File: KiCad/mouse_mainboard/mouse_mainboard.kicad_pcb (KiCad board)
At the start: 2 copper layers, 40.1 x 59.9 mm, 86 parts, among them J1 USB_OTG, J2 Conn_01x11_Male, Q1 BC807, Q10 BC807, Q11 BC817, Q12 BC807, Q13 BC817, Q14 BC817, Q2 BC807, Q3 BC817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

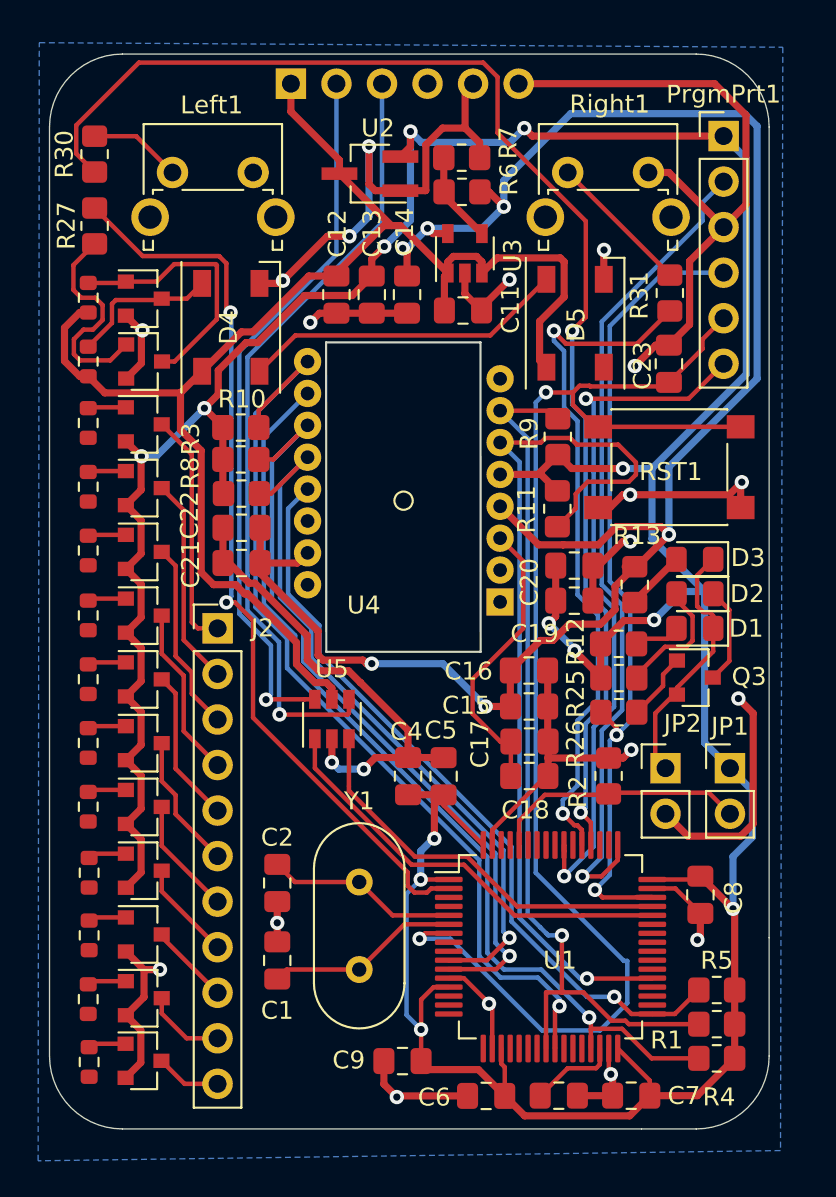
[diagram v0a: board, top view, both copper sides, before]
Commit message: Added test points
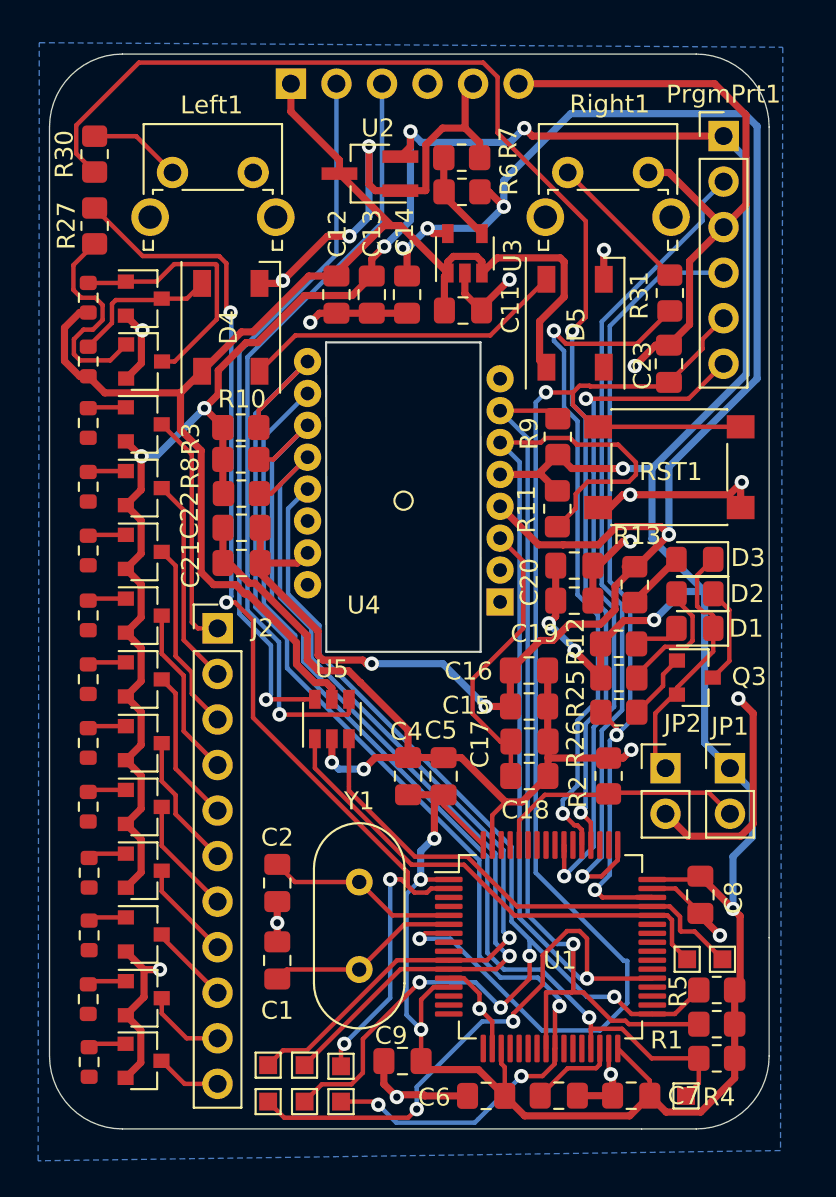
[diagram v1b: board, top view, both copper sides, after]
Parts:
- added TP1: TestPoint, TestPoint:TestPoint_Pad_1.0x1.0mm, F.Cu at (138.2, 128.5)
- added TP2: TestPoint, TestPoint:TestPoint_Pad_1.0x1.0mm, F.Cu at (136.1, 128.5)
- added TP3: TestPoint, TestPoint:TestPoint_Pad_1.0x1.0mm, F.Cu at (140.2, 130.6)
- added TP4: TestPoint, TestPoint:TestPoint_Pad_1.0x1.0mm, F.Cu at (136.1, 130.6)
- added TP5: TestPoint, TestPoint:TestPoint_Pad_1.0x1.0mm, F.Cu at (140.2, 128.6)
- added TP6: TestPoint, TestPoint:TestPoint_Pad_1.0x1.0mm, F.Cu at (159.5, 122.6)
- added TP7: TestPoint, TestPoint:TestPoint_Pad_1.0x1.0mm, F.Cu at (161.5, 122.6)
- added TP8: TestPoint, TestPoint:TestPoint_Pad_1.0x1.0mm, F.Cu at (159.4, 130.2)
- added TP9: TestPoint, TestPoint:TestPoint_Pad_1.0x1.0mm, F.Cu at (138.2, 130.6)
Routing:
- net pwm_gpo: track 50.8 -> 77.6 mm, vias 1 -> 3
- net ncs: track 42.9 -> 62.7 mm, vias 1 -> 4
- net pwm_int: track 52.7 -> 67.3 mm, vias 1 -> 3
- net led_d: track 50.6 -> 63.3 mm, vias 2 -> 4
- net miso: track 40.4 -> 52.9 mm
- net mosi: track 43.2 -> 53.4 mm
- net usb_d+: track 22.5 -> 28.1 mm
- net GND: track 182.1 -> 187.4 mm
- net usb_d-: track 23.9 -> 27.6 mm
- net sclk: track 53.0 -> 55.4 mm
- net mcu_cap: track 224.1 -> 225.9 mm

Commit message: Added pot strip port
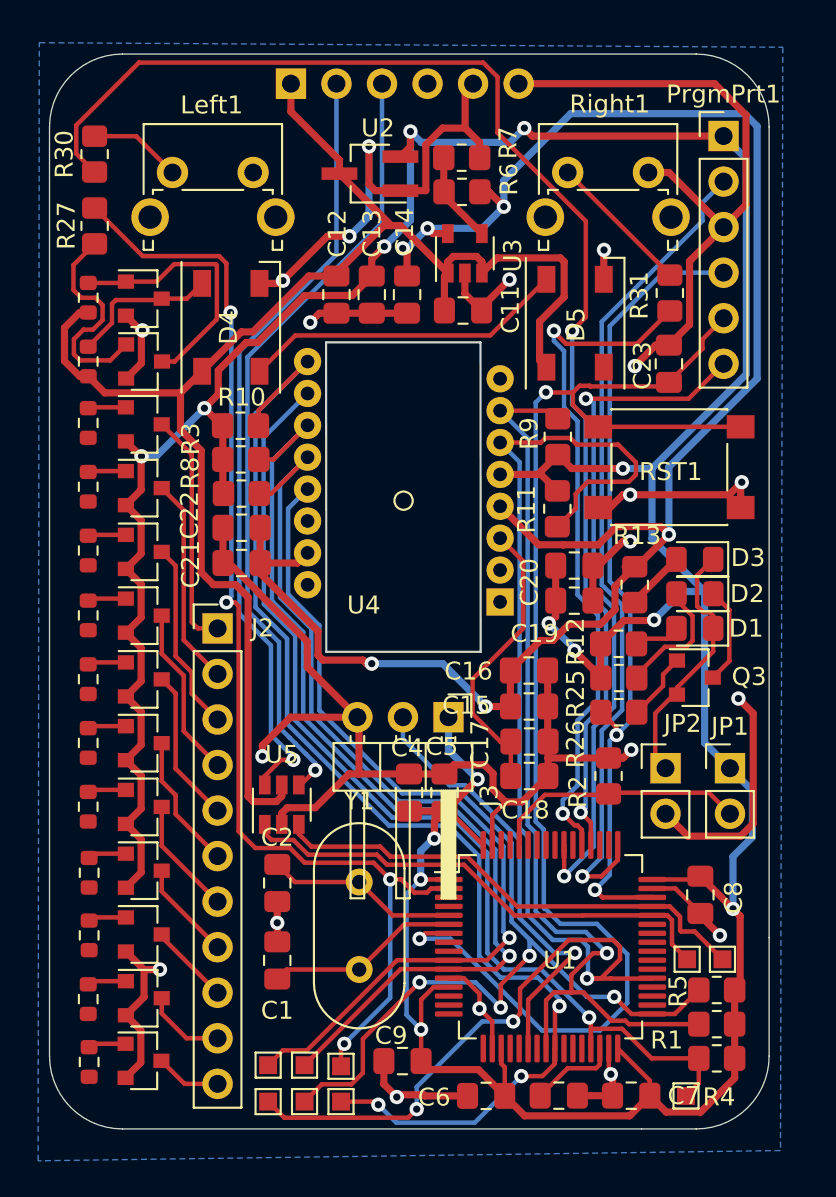
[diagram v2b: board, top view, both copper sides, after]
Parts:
- added J3: Conn_01x03_Male, Connector_PinHeader_2.54mm:PinHeader_1x03_P2.54mm_Horizontal, F.Cu at (146.2, 109.1)
- moved U5 5.53 mm to (136.9, 114.0)
- moved C4 0.92 mm to (144.0, 113.3)
- moved C5 0.92 mm to (146.0, 113.3)
- moved R10 0.10 mm to (134.6, 92.9)
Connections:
- U1 pad 22: Net-(U1-Pad22) -> strip_out
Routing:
- net strip_out: track 0.00 -> 24.7 mm, vias 0 -> 1
- net GND: track 187.4 -> 195.8 mm, vias 21 -> 20
- net +5V: track 80.2 -> 85.9 mm
- net mcu_cap: track 225.9 -> 231.5 mm, vias 13 -> 14
- net Net-(J1-Pad2): track 40.2 -> 43.7 mm
- net pwm_gpo: track 77.6 -> 80.3 mm
- net led_d: track 63.3 -> 65.9 mm
- net pwm_rst: track 50.5 -> 52.7 mm
- net pwm_int: track 67.3 -> 69.2 mm
- net mosi: track 53.4 -> 55.4 mm
- net sclk: track 55.4 -> 57.4 mm
- net miso: track 52.9 -> 54.9 mm
- net ncs: track 62.7 -> 64.6 mm
- net sw_rst: track 75.2 -> 76.3 mm
- net usb_d+: track 28.1 -> 27.5 mm
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
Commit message: Add layer, fixed references and added logo
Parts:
- added REF**: Utbult-design-logo, e7020e_custom_footprint_lib:Utbult-design-logo, B.Cu at (157.5, 99.1)
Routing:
- net GND: track 195.8 -> 185.0 mm
- added copper zone on F.Cu, net GND
- added copper zone on In1.Cu, net GND
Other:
- copper layers 2 -> 4

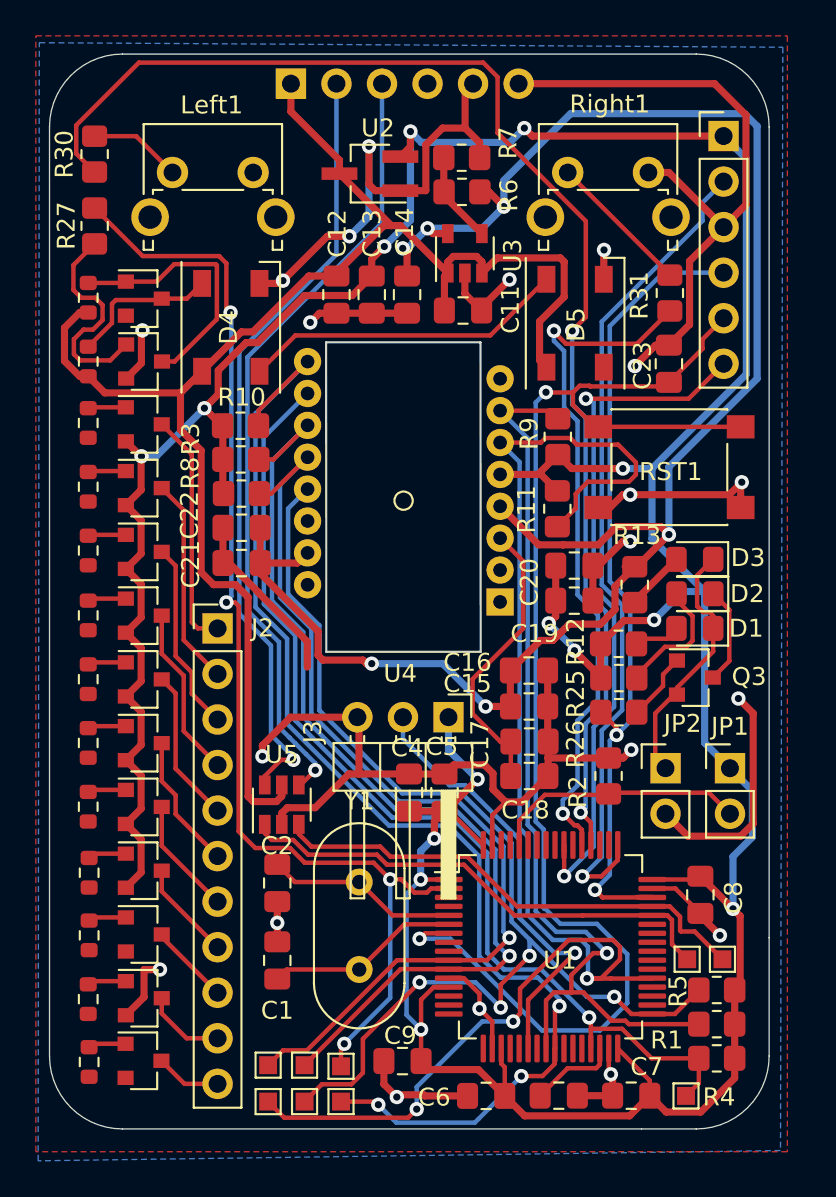
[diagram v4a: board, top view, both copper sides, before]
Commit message: Connected display
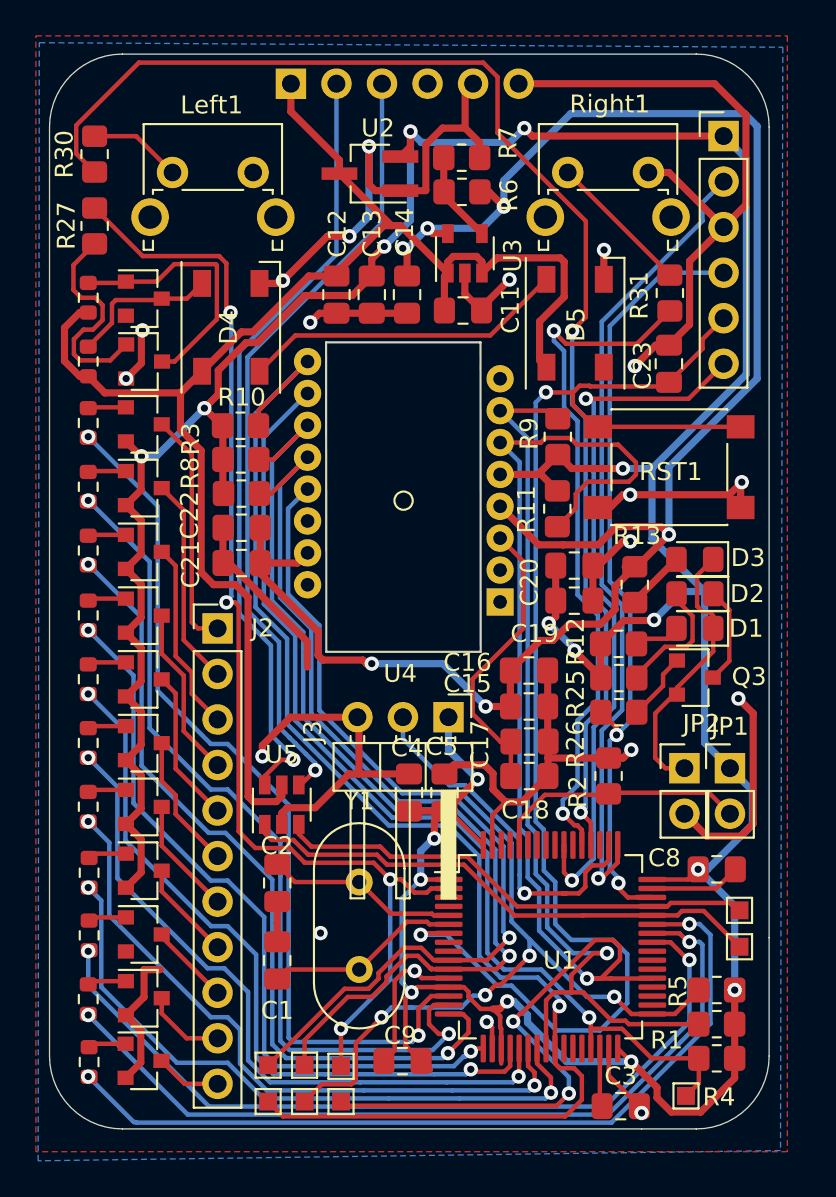
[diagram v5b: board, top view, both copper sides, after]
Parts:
- removed C6, C7: 100n, Capacitor_SMD:C_0805_2012Metric_Pad1.18x1.45mm_HandSolder
- C1, C2: value 22p -> 47p
- moved TP3 4.06 mm to (136.1, 130.6)
- moved TP4 4.06 mm to (140.2, 130.6)
- moved C3 3.50 mm to (155.8, 130.8)
- moved TP6 3.00 mm to (162.4, 121.9)
- moved TP7 2.89 mm to (162.4, 119.9)
- moved C8 1.69 mm to (161.2, 117.6), turned to 180 degrees
- moved JP2 1.05 mm to (159.4, 112.0)
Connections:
- U1 pad 14: Net-(U1-Pad14) -> disp_1
- U1 pad 15: Net-(U1-Pad15) -> disp_2
- U1 pad 16: Net-(U1-Pad16) -> disp_3
- U1 pad 17: Net-(U1-Pad17) -> disp_4
- U1 pad 20: Net-(U1-Pad20) -> disp_5
- U1 pad 21: Net-(U1-Pad21) -> disp_6
- U1 pad 22: strip_out -> disp_7
- U1 pad 23: Net-(U1-Pad23) -> disp_8
- U1 pad 41: Net-(U1-Pad41) -> disp_d1
- U1 pad 42: Net-(U1-Pad42) -> disp_d2
- U1 pad 43: Net-(U1-Pad43) -> disp_d3
- U1 pad 50: Net-(U1-Pad50) -> strip_out
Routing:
- net disp_1: track 0.00 -> 49.7 mm, vias 0 -> 2
- net disp_2: track 0.00 -> 48.5 mm, vias 0 -> 2
- net disp_d3: track 0.00 -> 46.6 mm, vias 0 -> 2
- net disp_d1: track 0.00 -> 46.2 mm, vias 0 -> 2
- net disp_d2: track 0.00 -> 46.1 mm, vias 0 -> 2
- net disp_3: track 0.00 -> 45.4 mm, vias 0 -> 2
- net disp_4: track 0.00 -> 41.1 mm, vias 0 -> 2
- net disp_5: track 0.00 -> 40.5 mm, vias 0 -> 2
- net disp_6: track 0.00 -> 38.4 mm, vias 0 -> 2
- net disp_7: track 0.00 -> 36.9 mm, vias 0 -> 2
- net disp_8: track 0.00 -> 36.5 mm, vias 0 -> 2
- net pwm_int: track 69.2 -> 76.8 mm, vias 3 -> 1
- net strip_out: track 24.7 -> 20.1 mm
- net mosi: track 55.4 -> 57.5 mm
- net usb_d-: track 27.8 -> 29.8 mm
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- added copper zone on In2.Cu, net (none)

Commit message: Fixed footprints
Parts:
- removed U5: USBLC6-2SC6, Package_TO_SOT_SMD:SOT-23-6
- J3: footprint Connector_PinHeader_2.54mm:PinHeader_1x03_P2.54mm_Horizontal -> Connector_PinHeader_2.54mm:PinHeader_1x03_P2.54mm_Vertical
- moved C4 0.11 mm to (143.9, 113.3)
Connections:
- J1 pad 2: Net-(J1-Pad2) -> usb_d-
- J1 pad 3: Net-(J1-Pad3) -> usb_d+
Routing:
- net Net-(J1-Pad3): track 44.3 -> 0.00 mm, vias 1 -> 0
- net Net-(J1-Pad2): track 43.7 -> 0.00 mm, vias 1 -> 0
- net usb_d+: track 27.0 -> 70.4 mm, vias 0 -> 1
- net usb_d-: track 29.8 -> 71.0 mm, vias 0 -> 1
- net +5V: track 85.9 -> 58.4 mm
- net GND: track 183.9 -> 182.9 mm, vias 19 -> 20
- added copper zone on In2.Cu, net GND
- removed copper zone on In2.Cu, net (none)
